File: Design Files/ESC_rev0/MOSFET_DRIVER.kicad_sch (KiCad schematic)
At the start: 38 parts, among them U5 DRV8302DCA

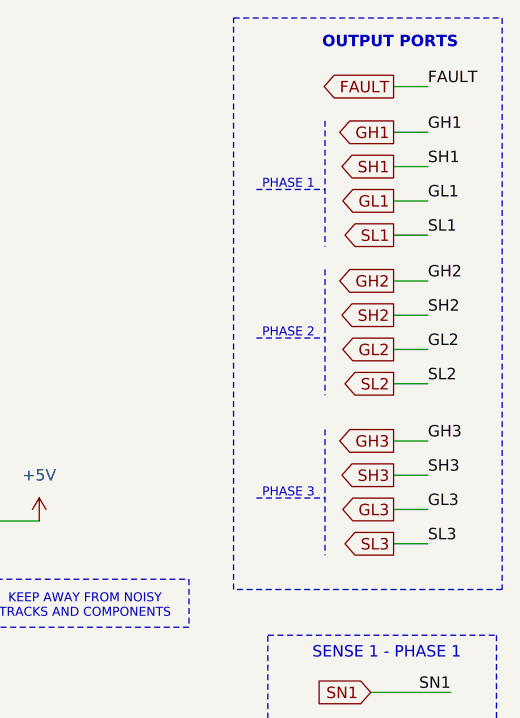
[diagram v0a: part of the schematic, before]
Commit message: update 13
assigned all footprints (provisionally) and imported them - errors and warning occurred, must be corrected in the future
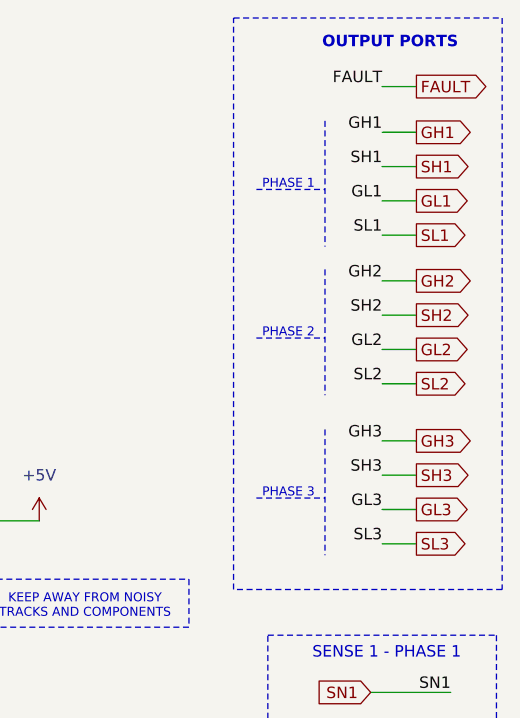
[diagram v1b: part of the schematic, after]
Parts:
- R15, R16, R17, R18, R19, R20, R21, R22, R23, R24, R25, R26: footprint (none) -> Resistor_SMD:R_0603_1608Metric

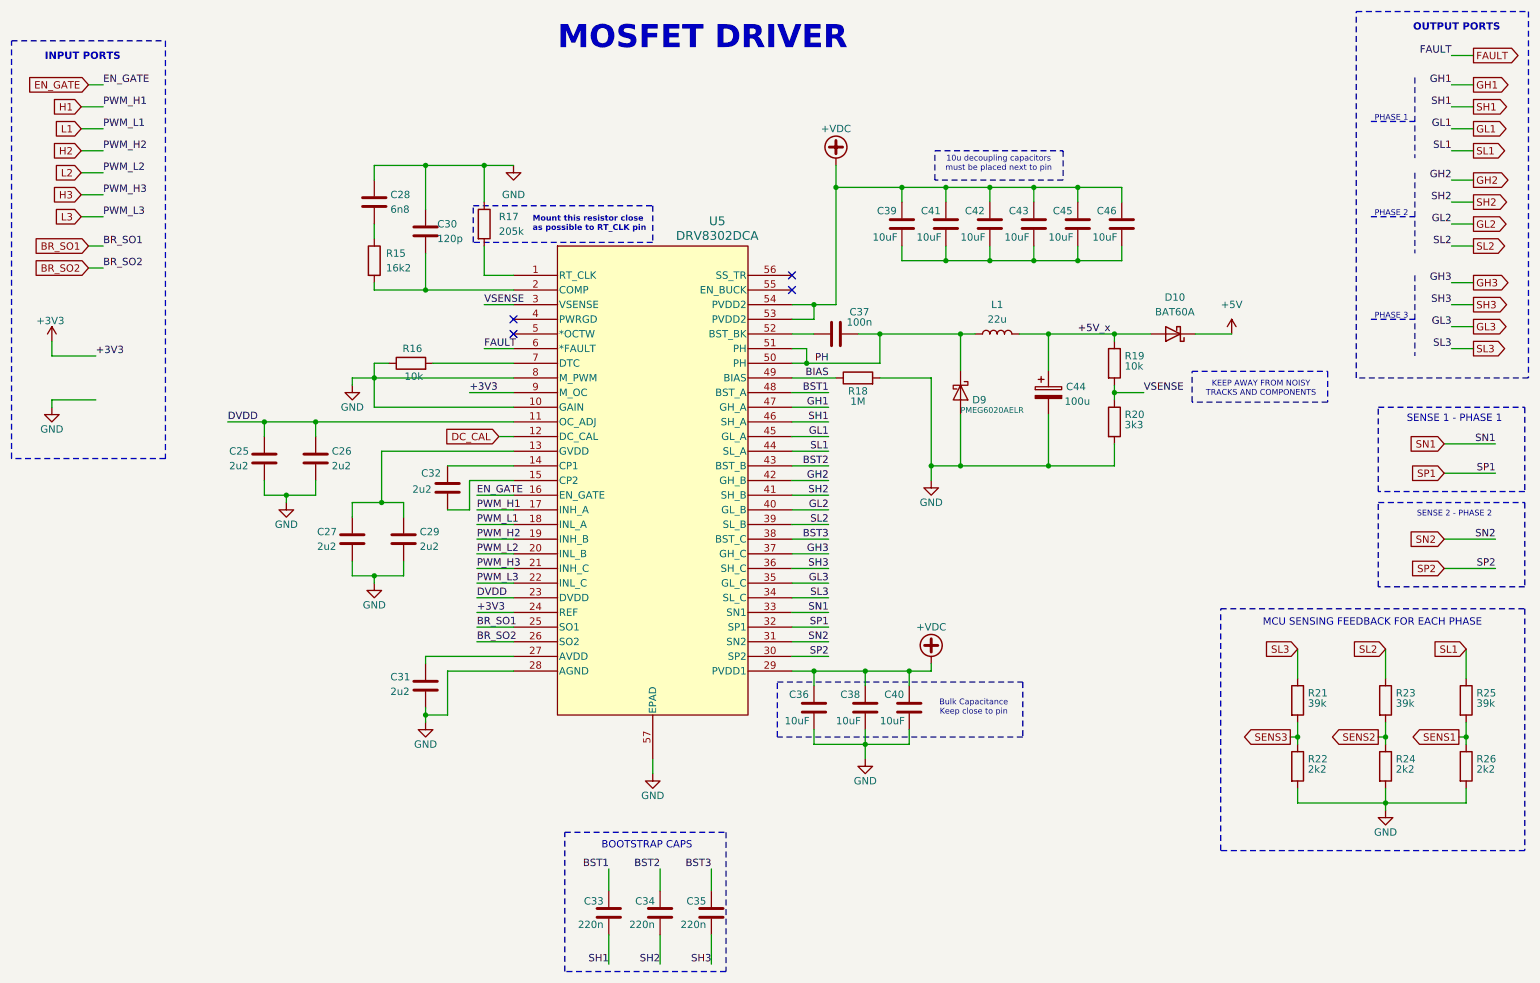
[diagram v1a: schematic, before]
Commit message: update 16
All components placed on board. Some components modifications and addition were made: added 3D models, changed some symbols and footprints positions and some component types.
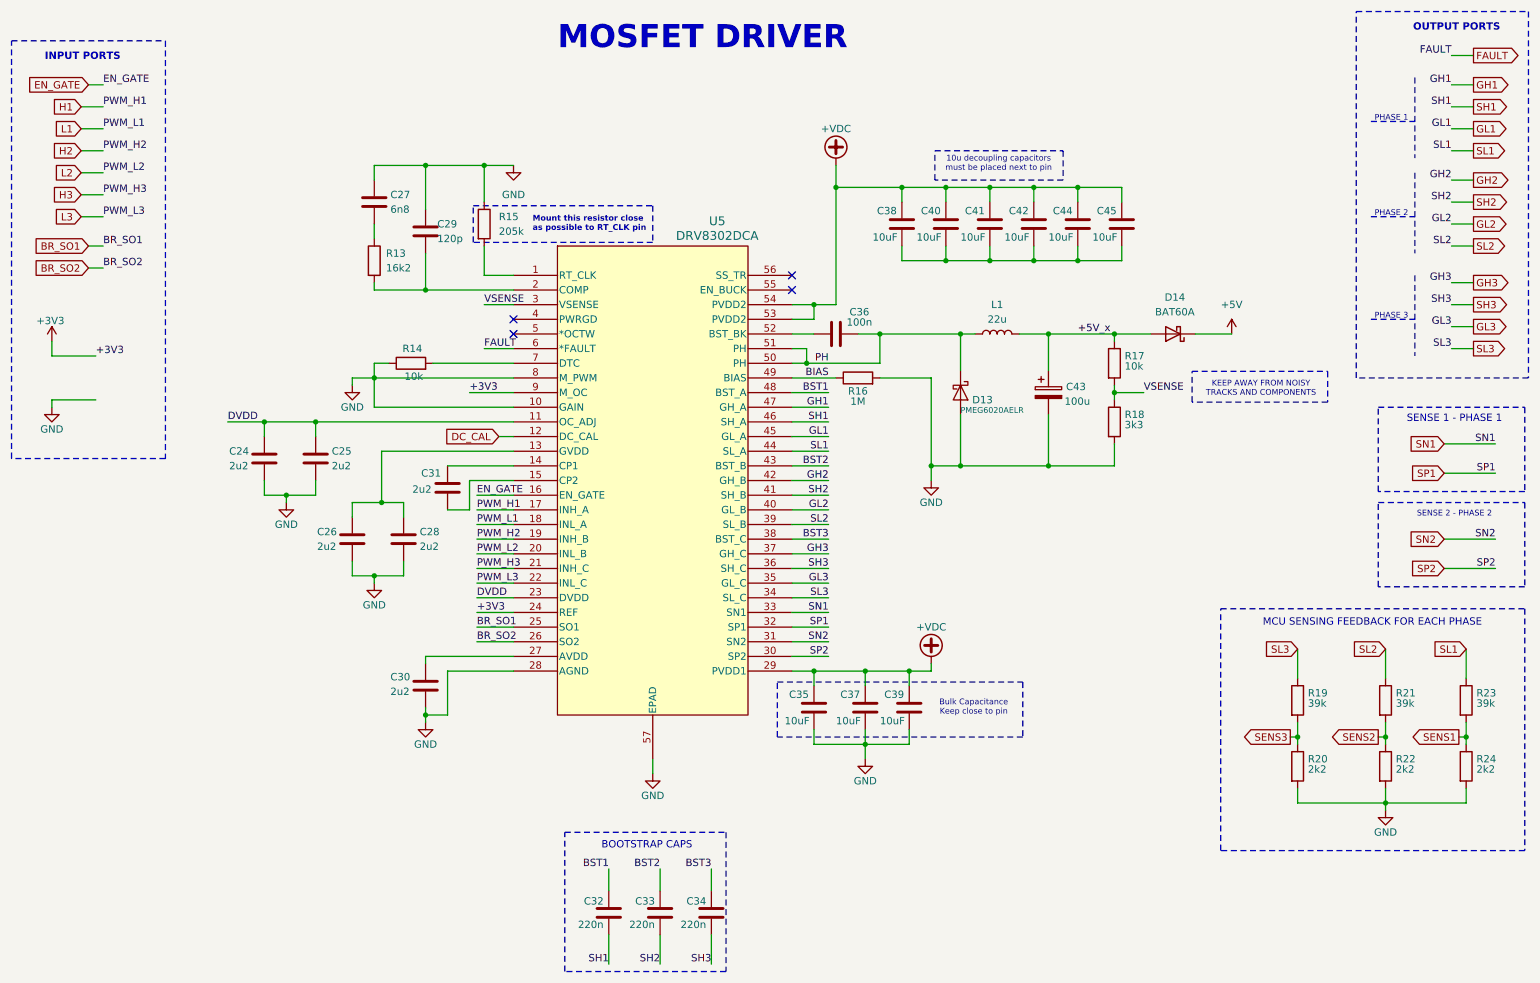
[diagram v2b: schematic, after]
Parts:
- C24: renamed from C25; footprint Capacitor_SMD:C_0201_0603Metric -> Capacitor_SMD:C_0603_1608Metric
- C25: renamed from C26; footprint Capacitor_SMD:C_0201_0603Metric -> Capacitor_SMD:C_0603_1608Metric
- C26: renamed from C27; footprint Capacitor_SMD:C_0201_0603Metric -> Capacitor_SMD:C_0603_1608Metric
- C27: renamed from C28; footprint Capacitor_SMD:C_0201_0603Metric -> Capacitor_SMD:C_0603_1608Metric
- C28: renamed from C29; footprint Capacitor_SMD:C_0201_0603Metric -> Capacitor_SMD:C_0603_1608Metric
- C29: renamed from C30; footprint Capacitor_SMD:C_0201_0603Metric -> Capacitor_SMD:C_0603_1608Metric
- C30: renamed from C31; footprint Capacitor_SMD:C_0201_0603Metric -> Capacitor_SMD:C_0603_1608Metric
- C31: renamed from C32; footprint Capacitor_SMD:C_0201_0603Metric -> Capacitor_SMD:C_0603_1608Metric
- C32: renamed from C33; footprint Capacitor_SMD:C_0201_0603Metric -> Capacitor_SMD:C_0603_1608Metric
- C33: renamed from C34; footprint Capacitor_SMD:C_0201_0603Metric -> Capacitor_SMD:C_0603_1608Metric
- C34: renamed from C35; footprint Capacitor_SMD:C_0201_0603Metric -> Capacitor_SMD:C_0603_1608Metric
- C35: renamed from C36; footprint Capacitor_SMD:C_0201_0603Metric -> Capacitor_SMD:C_0603_1608Metric
- C36: renamed from C37; footprint Capacitor_SMD:C_0201_0603Metric -> Capacitor_SMD:C_0603_1608Metric
- C37: renamed from C38; footprint Capacitor_SMD:C_0201_0603Metric -> Capacitor_SMD:C_0603_1608Metric
- C38: renamed from C39; footprint Capacitor_SMD:C_0201_0603Metric -> Capacitor_SMD:C_0603_1608Metric
- C39: renamed from C40; footprint Capacitor_SMD:C_0201_0603Metric -> Capacitor_SMD:C_0603_1608Metric
- C40: renamed from C41; footprint Capacitor_SMD:C_0201_0603Metric -> Capacitor_SMD:C_0603_1608Metric
- C41: renamed from C42; footprint Capacitor_SMD:C_0201_0603Metric -> Capacitor_SMD:C_0603_1608Metric
- C42: renamed from C43; footprint Capacitor_SMD:C_0201_0603Metric -> Capacitor_SMD:C_0603_1608Metric
- C43: renamed from C44; footprint Capacitor_SMD:C_0201_0603Metric -> Capacitor_SMD:C_1210_3225Metric
- C44: renamed from C45; footprint Capacitor_SMD:C_0201_0603Metric -> Capacitor_SMD:C_0603_1608Metric
- C45: renamed from C46; footprint Capacitor_SMD:C_0201_0603Metric -> Capacitor_SMD:C_0603_1608Metric
- renumbered D9 to D13, D10 to D14, R15 to R13, R16 to R14, R17 to R15, R18 to R16, R19 to R17, R20 to R18, R21 to R19, R22 to R20, R23 to R21, R24 to R22, R25 to R23, R26 to R24

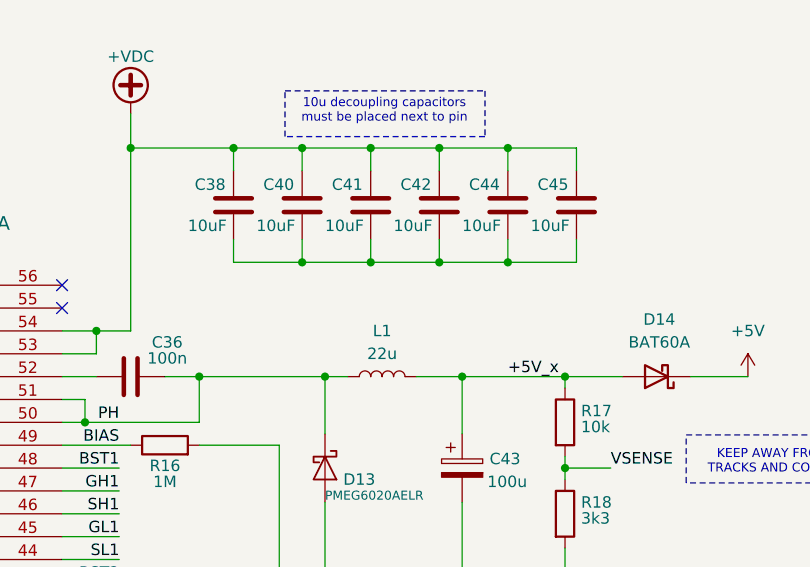
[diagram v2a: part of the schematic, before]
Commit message: update 18
Route process partially complete. Some corrections were made in footprints and pins references. Probably the power lines will need changes in size.
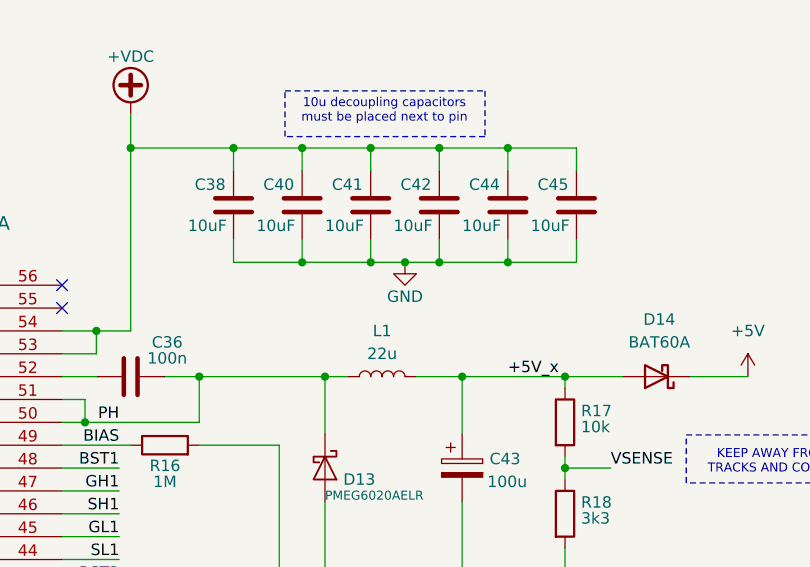
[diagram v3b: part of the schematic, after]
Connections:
- net GND: now also C38.2, C40.2, C41.2, C42.2, C44.2, C45.2
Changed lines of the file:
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@@
 	)
 	(junction
+		(at 193.04 59.69)
+		(diameter 0)
+		(color 0 0 0 0)
+	)
+	(junction
 		(at 91.44 64.77)
 		(diameter 0)
@@
 	(wire
 		(pts
-			(xy 189.23 59.69) (xy 196.85 59.69)
+			(xy 189.23 59.69) (xy 193.04 59.69)
 		)
 		(stroke
@@
 	(wire
 		(pts
+			(xy 193.04 59.69) (xy 196.85 59.69)
+		)
+		(stroke
+			(width 0)
+			(type default)
+		)
+	)
+	(wire
+		(pts
 			(xy 26.67 83.82) (xy 26.67 85.09)
 		)
@@
 					(unit 1)
 				)
+			)
+		)
+	)
+	(symbol
+		(lib_id "power:GND")
+		(at 193.04 59.69 0)
+		(unit 1)
+		(exclude_from_sim no)
+		(in_bom yes)
+		(on_board yes)
+		(dnp no)
+		(property "Reference" "#PWR086"
+			(at 193.04 66.04 0)
+			(effects
+				(font
+					(size 1.27 1.27)
+				)
+				(hide yes)
+			)
+		)
+		(property "Value" "GND"
+			(at 193.04 63.5 0)
+			(effects
+				(font
+					(size 1.27 1.27)
+				)
+			)
+		)
+		(property "Footprint" ""
+			(at 193.04 59.69 0)
+			(effects
+				(font
+					(size 1.27 1.27)
+				)
+				(hide yes)
+			)
+		)
+		(property "Datasheet" ""
+			(at 193.04 59.69 0)
+			(effects
+				(font
+					(size 1.27 1.27)
+				)
+				(hide yes)
+			)
+		)
+		(property "Description" "Power symbol creates a global label with name \"GND\" , ground"
+			(at 193.04 59.69 0)
+			(effects
+				(font
+					(size 1.27 1.27)
+				)
+				(hide yes)
+			)
+		)
+		(pin "1"
+		)
+		(instances
+			(project "ESC_rev0"
+				(path "/7906e740-34c4-4b06-b70f-1daa08872946/7bd23810-1284-43c0-85ae-fb85b4c95d04"
+					(reference "#PWR086")
+					(unit 1)
+				)
